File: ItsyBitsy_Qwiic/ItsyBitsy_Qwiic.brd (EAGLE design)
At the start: 52.7 x 20.3 mm, 5 parts

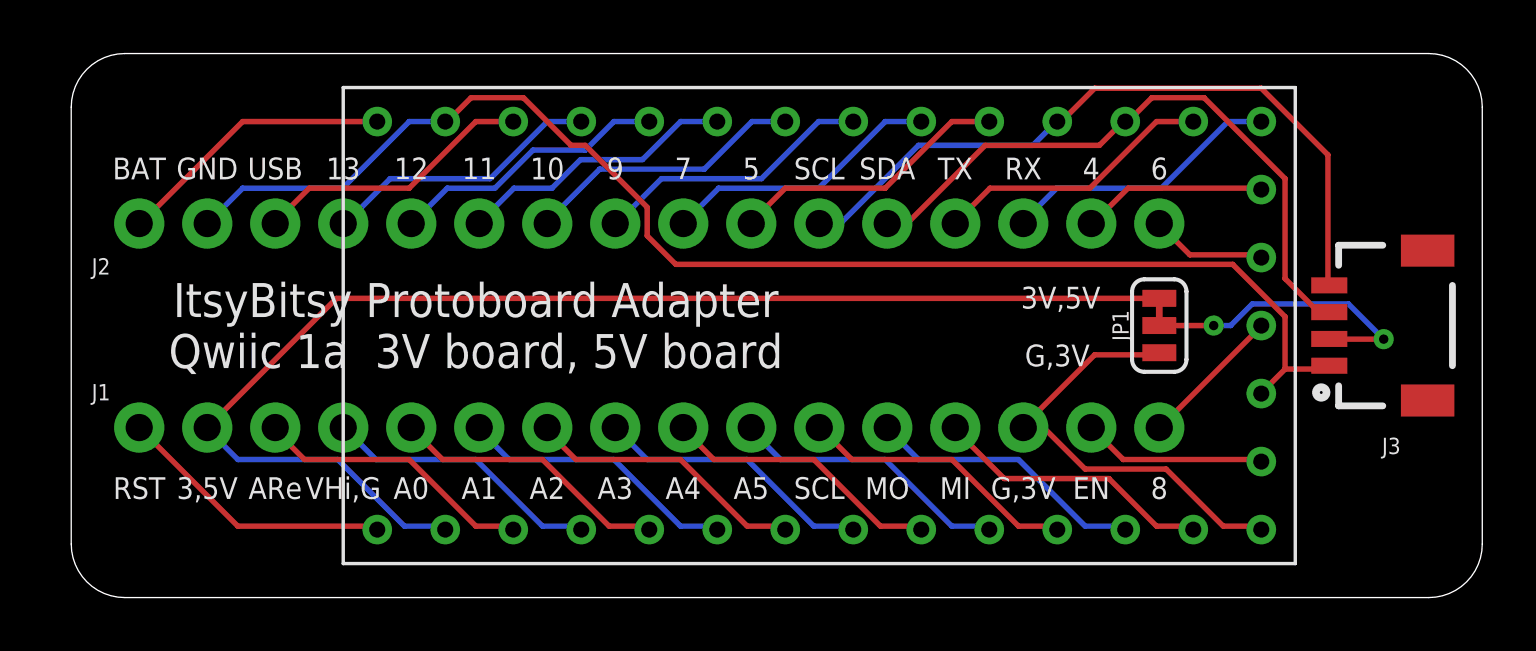
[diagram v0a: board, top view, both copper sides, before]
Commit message: enlarged ItsyBitsy holes, add CAM/Gerber zip file
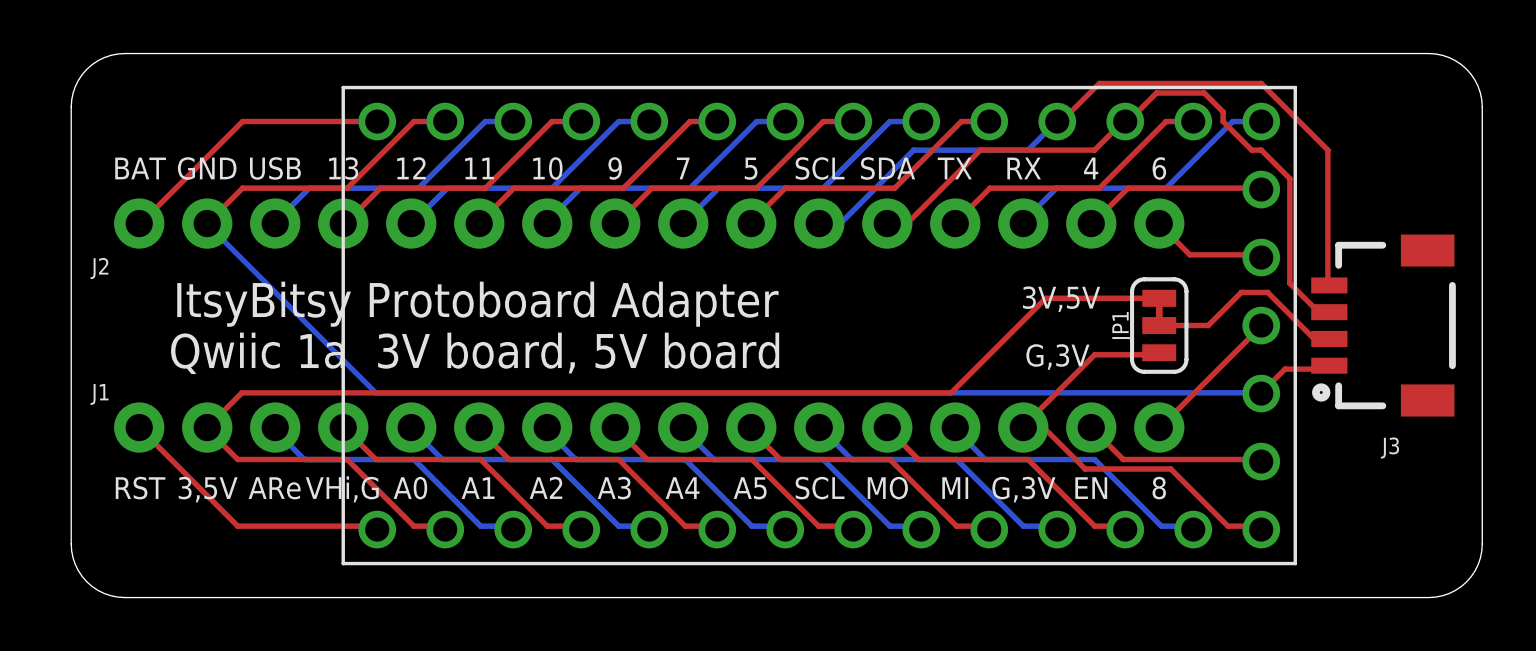
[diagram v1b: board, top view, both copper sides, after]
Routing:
- net GND: track 51.2 -> 55.5 mm
- net VCC-QWIIC: track 11.3 -> 7.58 mm, vias 2 -> 0
